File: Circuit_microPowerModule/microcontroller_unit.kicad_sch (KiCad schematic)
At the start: 30 parts, among them J201 USB_C_Receptacle_USB2.0, J202 Debug, SW201 KMR2, U201 W25Q128JVS, U202 RP2040, Y201 12MHz

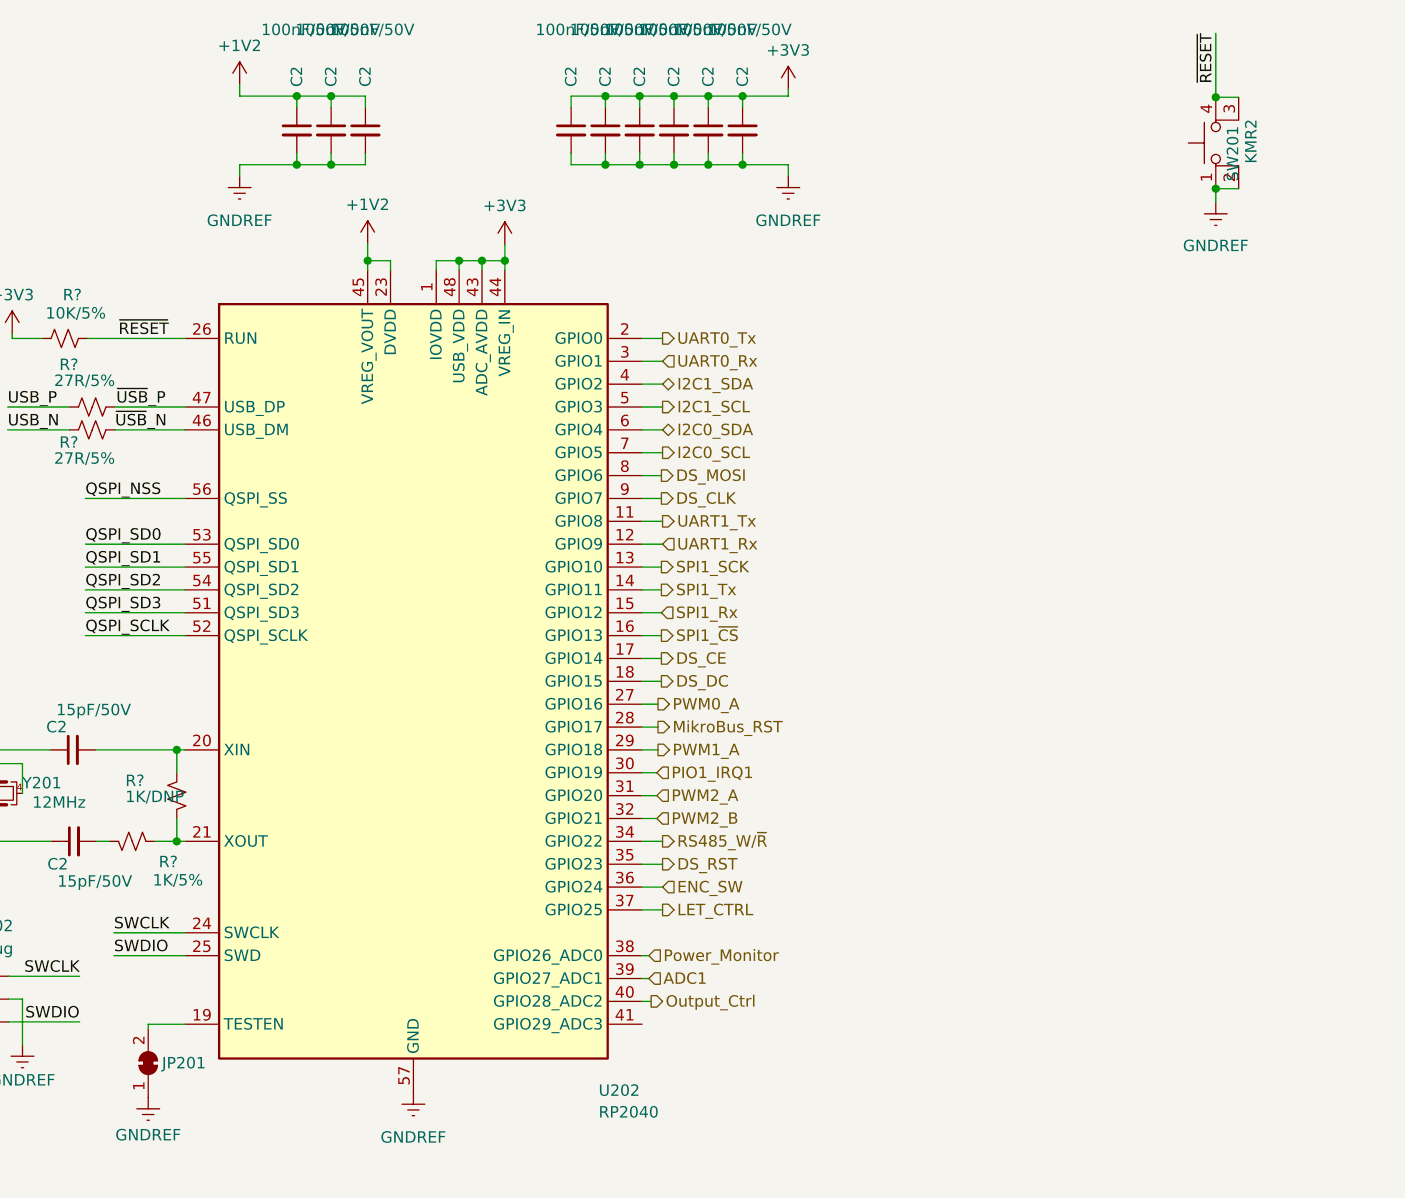
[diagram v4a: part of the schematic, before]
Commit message: added H-Bridge
Control load forward or reverse (current direction)
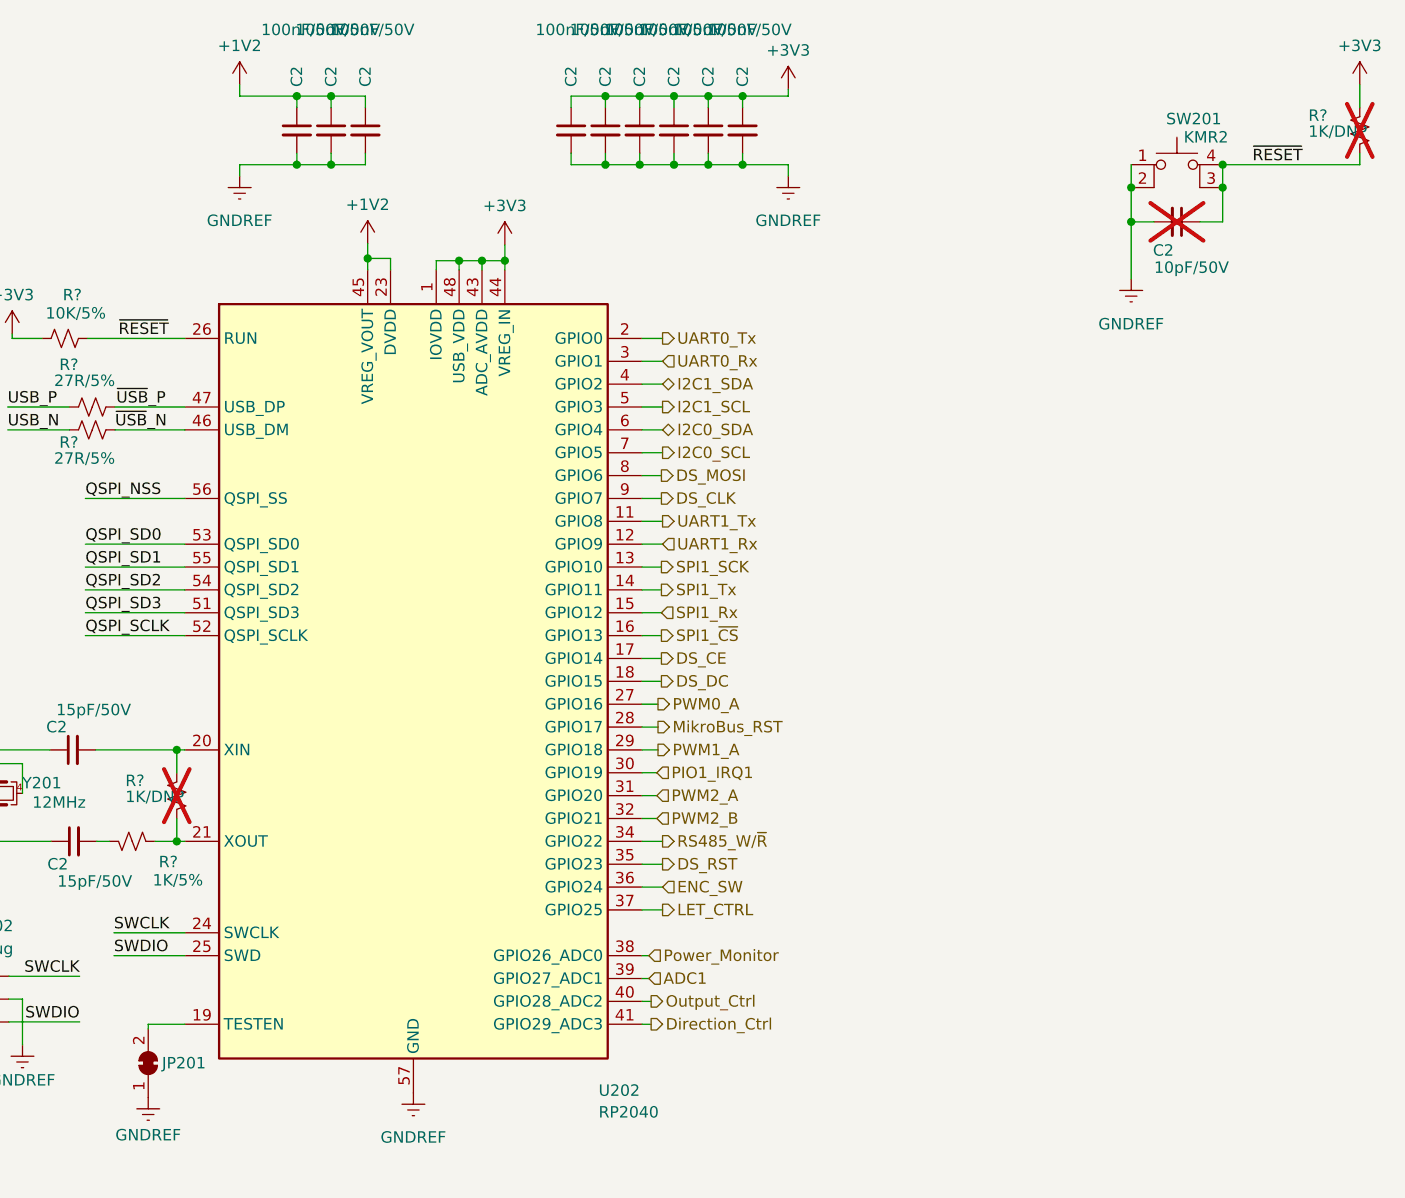
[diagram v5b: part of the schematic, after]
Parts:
- added C2: 10pF/50V, Capacitor_SMD:C_0603_1608Metric, symbol Device:C_Small
- added R?: 1K/DNP, Resistor_SMD:R_0603_1608Metric, symbol Device:R_Small_US
- R?: now not fitted
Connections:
- net +3V3: now also R?.1
- net GNDREF: now also C2.2
- net ~{RESET}: now also C2.1, R?.2
- net Direction_Ctrl: now reaches U202.41 (GPIO29_ADC3)
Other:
- moved on the sheet: SW201

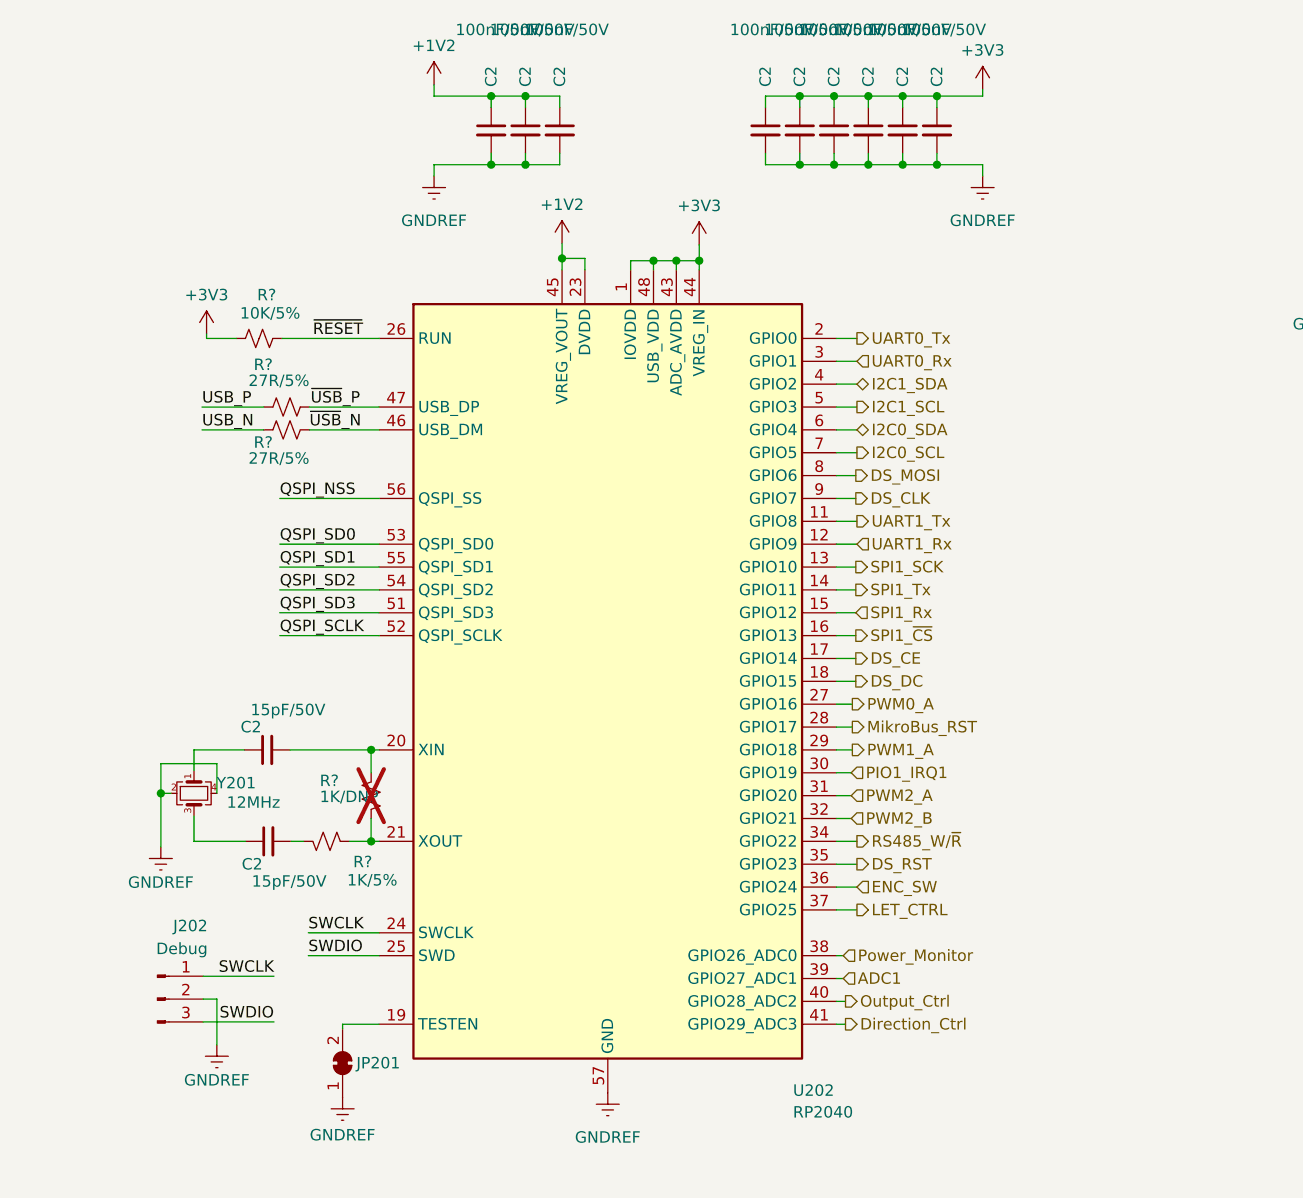
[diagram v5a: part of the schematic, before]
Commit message: modify ERC error, protect components
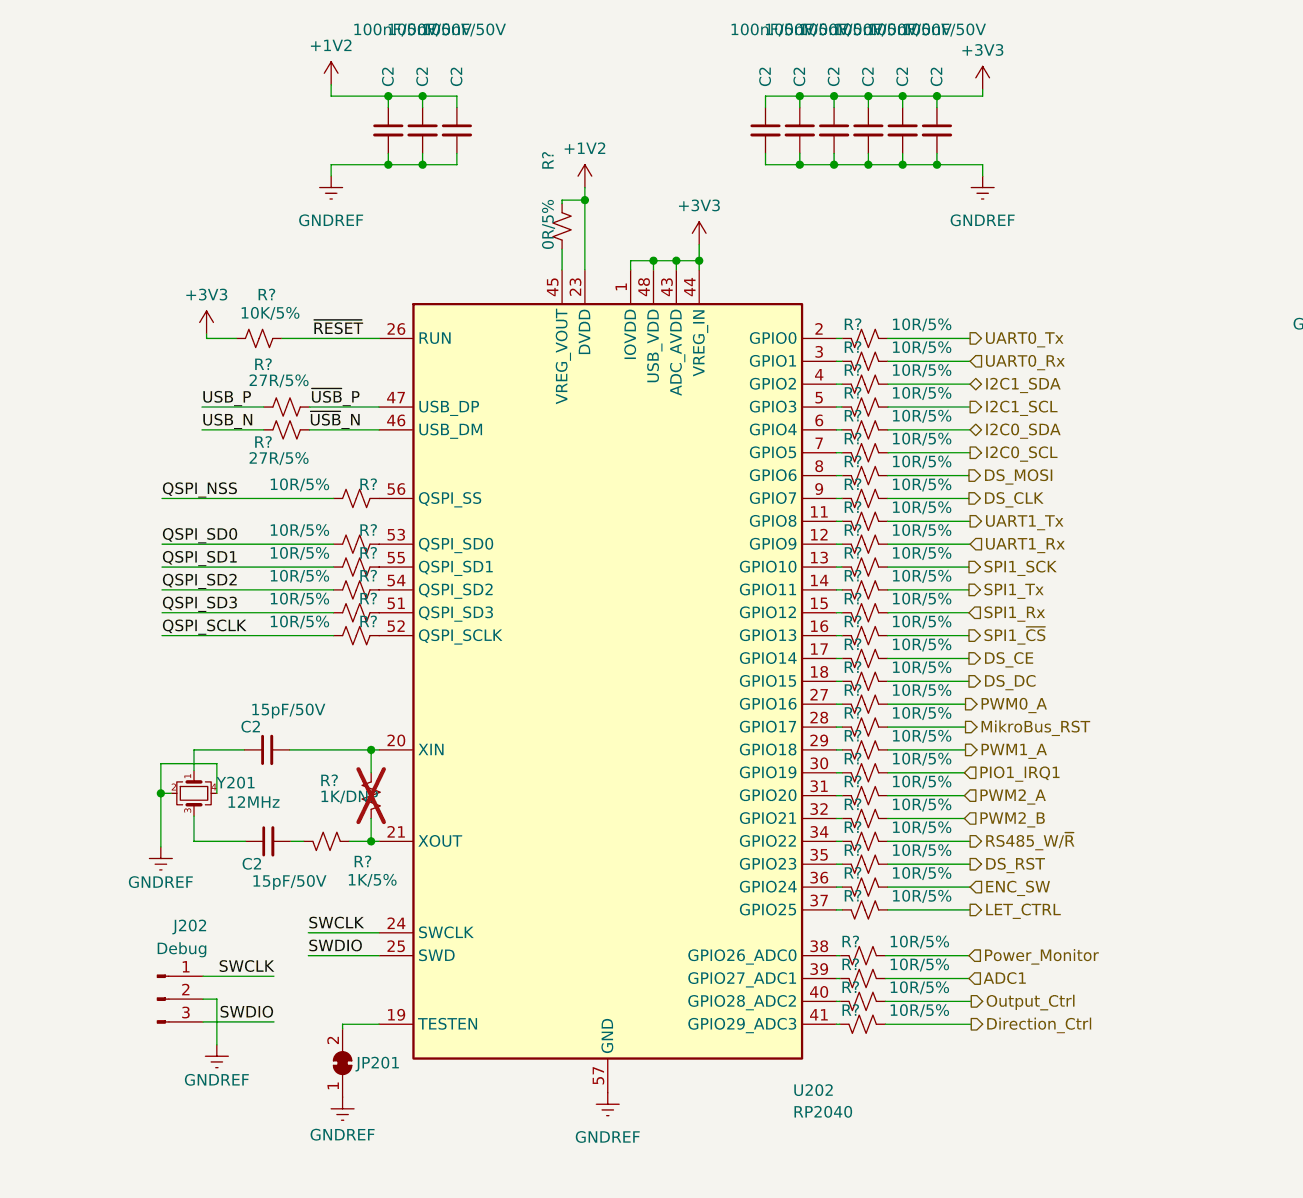
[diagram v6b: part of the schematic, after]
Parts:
- added R? (x36): 10R/5%, Resistor_SMD:R_0603_1608Metric, symbol Device:R_Small_US
- added R?: 0R/5%, Resistor_SMD:R_0603_1608Metric, symbol Device:R_Small_US
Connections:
- net +1V2: now also R?.1; no longer U202.45 (VREG_VOUT)
- net ADC1: now also R?.2; no longer U202.39 (GPIO27_ADC1)
- net DS_CE: now also R?.2; no longer U202.17 (GPIO14)
- net DS_CLK: now also R?.2; no longer U202.9 (GPIO7)
- net DS_DC: now also R?.2; no longer U202.18 (GPIO15)
- net DS_MOSI: now also R?.2; no longer U202.8 (GPIO6)
- net DS_RST: now also R?.2; no longer U202.35 (GPIO23)
- net Direction_Ctrl: now also R?.2; no longer U202.41 (GPIO29_ADC3)
- net ENC_SW: now also R?.2; no longer U202.36 (GPIO24)
- net I2C0_SCL: now also R?.2; no longer U202.7 (GPIO5)
- net I2C0_SDA: now also R?.2; no longer U202.6 (GPIO4)
- net I2C1_SCL: now also R?.2; no longer U202.5 (GPIO3)
- net I2C1_SDA: now also R?.2; no longer U202.4 (GPIO2)
- net LET_CTRL: now also R?.2; no longer U202.37 (GPIO25)
- net MikroBus_RST: now also R?.2; no longer U202.28 (GPIO17)
- net Output_Ctrl: now also R?.2; no longer U202.40 (GPIO28_ADC2)
- net PIO1_IRQ1: now also R?.2; no longer U202.30 (GPIO19)
- net PWM0_A: now also R?.2; no longer U202.27 (GPIO16)
- net PWM1_A: now also R?.2; no longer U202.29 (GPIO18)
- net PWM2_A: now also R?.2; no longer U202.31 (GPIO20)
- net PWM2_B: now also R?.2; no longer U202.32 (GPIO21)
- net Power_Monitor: now also R?.2; no longer U202.38 (GPIO26_ADC0)
- net QSPI_NSS: now also R?.2; no longer U202.56 (QSPI_SS)
- net QSPI_SCLK: now also R?.2; no longer U202.52 (QSPI_SCLK)
- net QSPI_SD0: now also R?.2; no longer U202.53 (QSPI_SD0)
- net QSPI_SD1: now also R?.2; no longer U202.55 (QSPI_SD1)
- net QSPI_SD2: now also R?.2; no longer U202.54 (QSPI_SD2)
- net QSPI_SD3: now also R?.2; no longer U202.51 (QSPI_SD3)
- net RS485_W/~{R}: now also R?.2; no longer U202.34 (GPIO22)
- net SPI1_Rx: now also R?.2; no longer U202.15 (GPIO12)
- net SPI1_SCK: now also R?.2; no longer U202.13 (GPIO10)
- net SPI1_Tx: now also R?.2; no longer U202.14 (GPIO11)
- net SPI1_~{CS}: now also R?.2; no longer U202.16 (GPIO13)
- net UART0_Rx: now also R?.2; no longer U202.3 (GPIO1)
- net UART0_Tx: now also R?.2; no longer U202.2 (GPIO0)
- net UART1_Rx: now also R?.2; no longer U202.12 (GPIO9)
- net UART1_Tx: now also R?.2; no longer U202.11 (GPIO8)
- new net: R?.1, U202.51 (QSPI_SD3)
- new net: R?.1, U202.34 (GPIO22)
- new net: R?.1, U202.8 (GPIO6)
- new net: R?.1, U202.16 (GPIO13)
- new net: R?.1, U202.27 (GPIO16)
- new net: R?.1, U202.36 (GPIO24)
- new net: R?.1, U202.52 (QSPI_SCLK)
- new net: R?.1, U202.18 (GPIO15)
- new net: R?.1, U202.6 (GPIO4)
- new net: R?.1, U202.4 (GPIO2)
- new net: R?.1, U202.12 (GPIO9)
- new net: R?.1, U202.11 (GPIO8)
- new net: R?.1, U202.13 (GPIO10)
- new net: R?.1, U202.14 (GPIO11)
- new net: R?.1, U202.15 (GPIO12)
- new net: R?.1, U202.17 (GPIO14)
- new net: R?.1, U202.2 (GPIO0)
- new net: R?.1, U202.28 (GPIO17)
- new net: R?.1, U202.29 (GPIO18)
- new net: R?.1, U202.3 (GPIO1)
- new net: R?.1, U202.30 (GPIO19)
- new net: R?.1, U202.31 (GPIO20)
- new net: R?.1, U202.32 (GPIO21)
- new net: R?.1, U202.35 (GPIO23)
- new net: R?.1, U202.37 (GPIO25)
- new net: R?.1, U202.38 (GPIO26_ADC0)
- new net: R?.1, U202.39 (GPIO27_ADC1)
- new net: R?.1, U202.40 (GPIO28_ADC2)
- new net: R?.1, U202.41 (GPIO29_ADC3)
- new net: R?.2, U202.45 (VREG_VOUT)
- new net: R?.1, U202.5 (GPIO3)
- new net: R?.1, U202.53 (QSPI_SD0)
- new net: R?.1, U202.54 (QSPI_SD2)
- new net: R?.1, U202.55 (QSPI_SD1)
- new net: R?.1, U202.56 (QSPI_SS)
- new net: R?.1, U202.7 (GPIO5)
- new net: R?.1, U202.9 (GPIO7)
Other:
- title: (none) -> µPower Module
- moved on the sheet: C2
